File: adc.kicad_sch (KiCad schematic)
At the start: 48 parts, among them J10 Conn_01x02_Pin, J4 Conn_01x03_Pin, J5 Conn_01x03_Pin, J6 Conn_01x02_Pin, J7 Conn_01x03_Pin, J8 Conn_01x02_Pin, J9 Conn_01x02_Pin, U9 LTC2299xUP

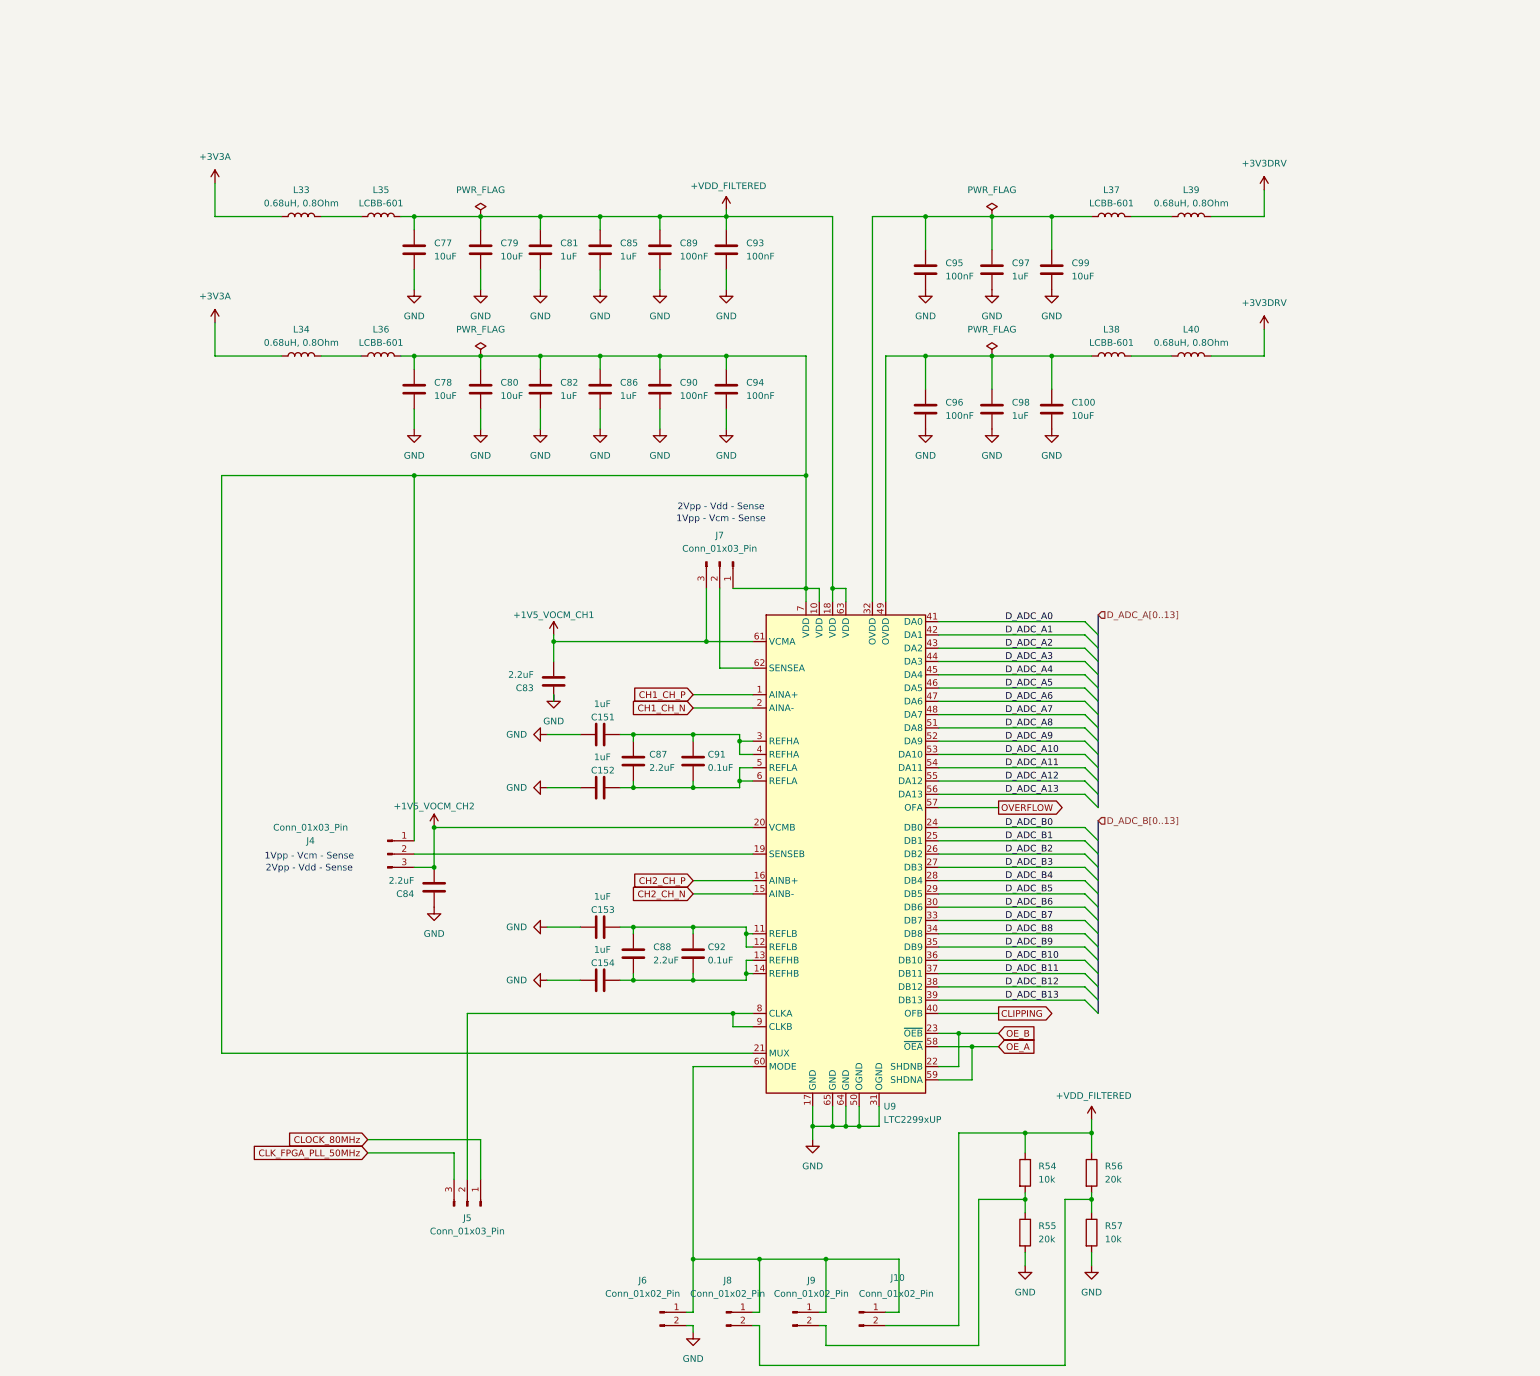
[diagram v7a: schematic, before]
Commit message: Interleaved channel 1 / channel 2
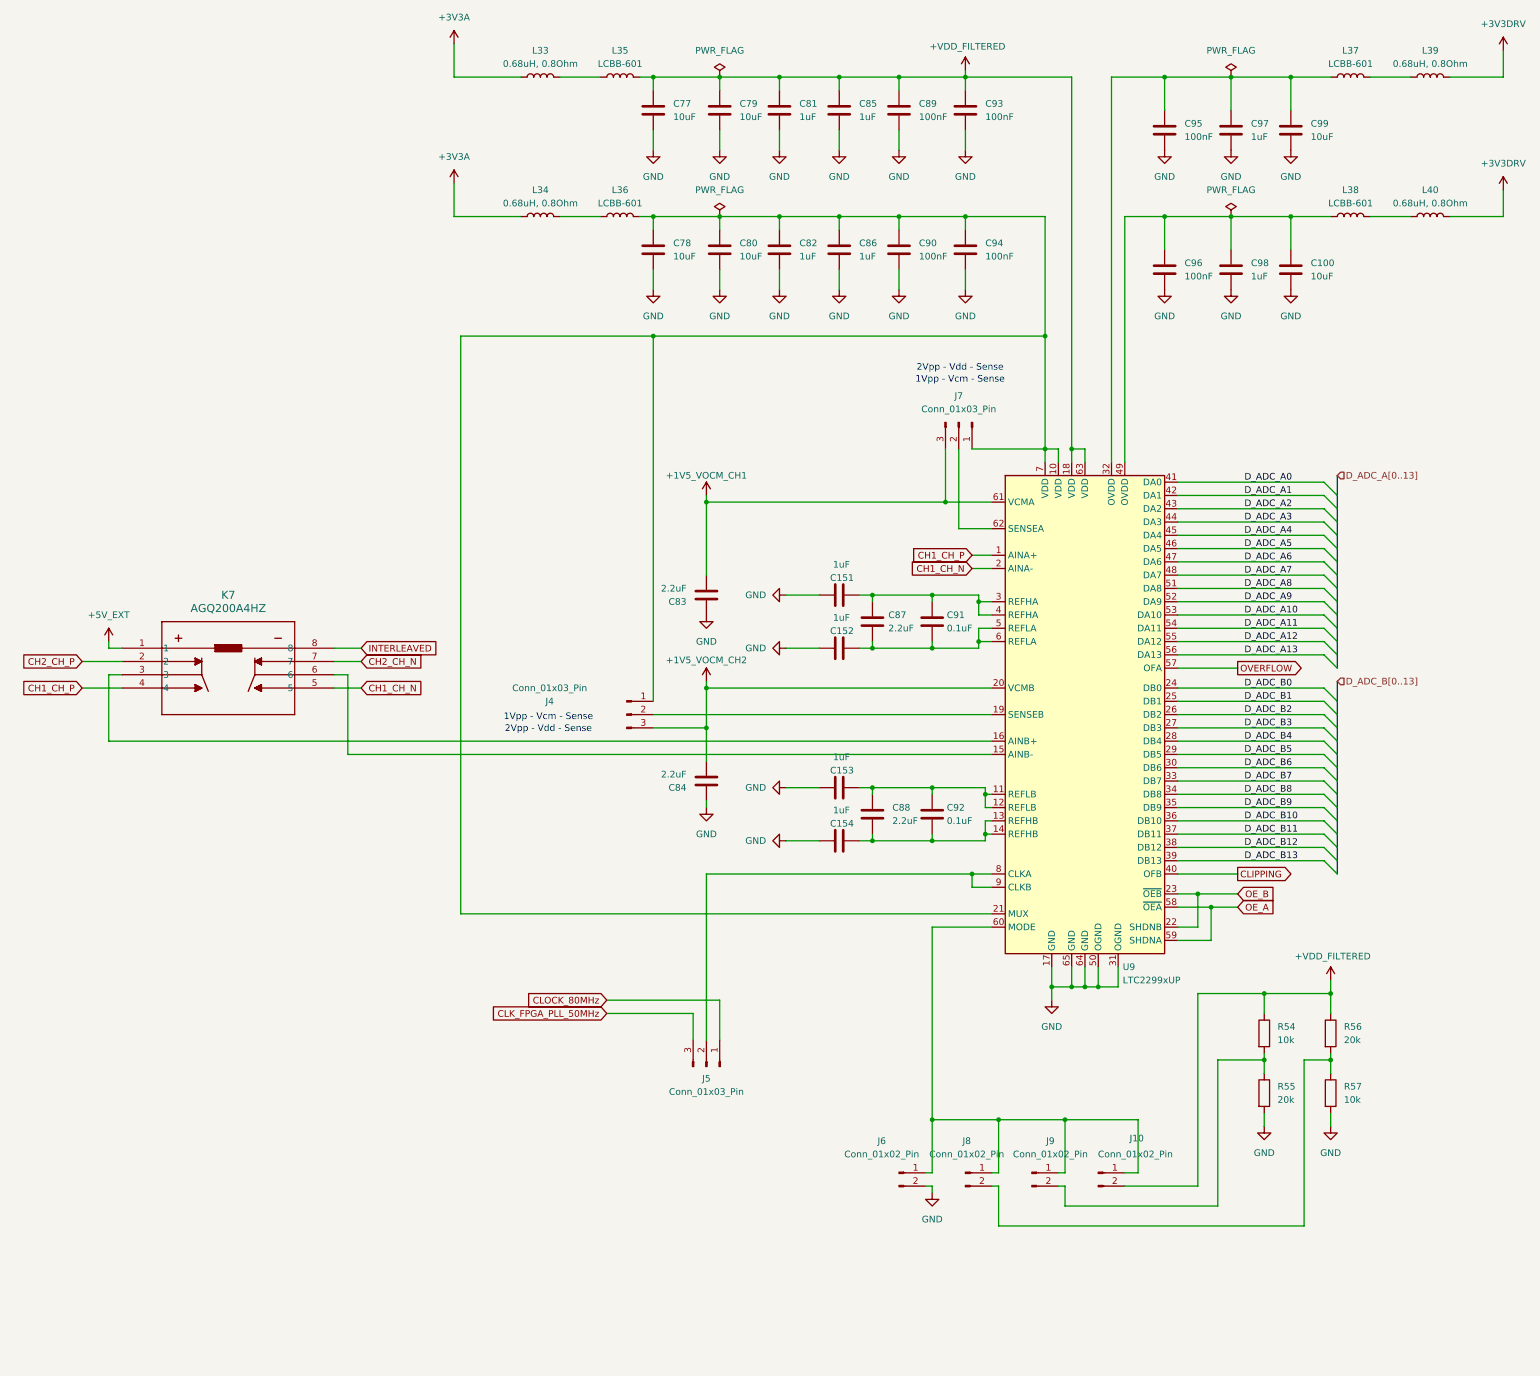
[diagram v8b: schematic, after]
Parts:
- added K7: AGQ200A4HZ, AGQ200A4H:RELAY_AGQ_A_PAN, symbol AGQ200A4H:AGQ200A4HZ
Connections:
- net CH1_CH_N: now also K7.5
- net CH1_CH_P: now also K7.4
- net CH2_CH_N: now also K7.7; no longer U9.15 (AINB-)
- net CH2_CH_P: now also K7.2; no longer U9.16 (AINB+)
- new net: K7.6, U9.15 (AINB-)
- new net: K7.3, U9.16 (AINB+)
- new net +5V_EXT: K7.1
- new net INTERLEAVED: K7.8
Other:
- moved on the sheet: C100, C151, C152, C153, C154, C77, C78, C79, C80, C81, C82, C83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
